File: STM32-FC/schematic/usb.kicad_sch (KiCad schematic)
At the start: 26 parts, among them J2 USB_C_USB2.0_16P, J3 BM06B-GHS-TBT, U1 USBLC6-2SC6, U2 TPS62840YBG, U3 TPS62840YBG, U4 TPS62840YBG

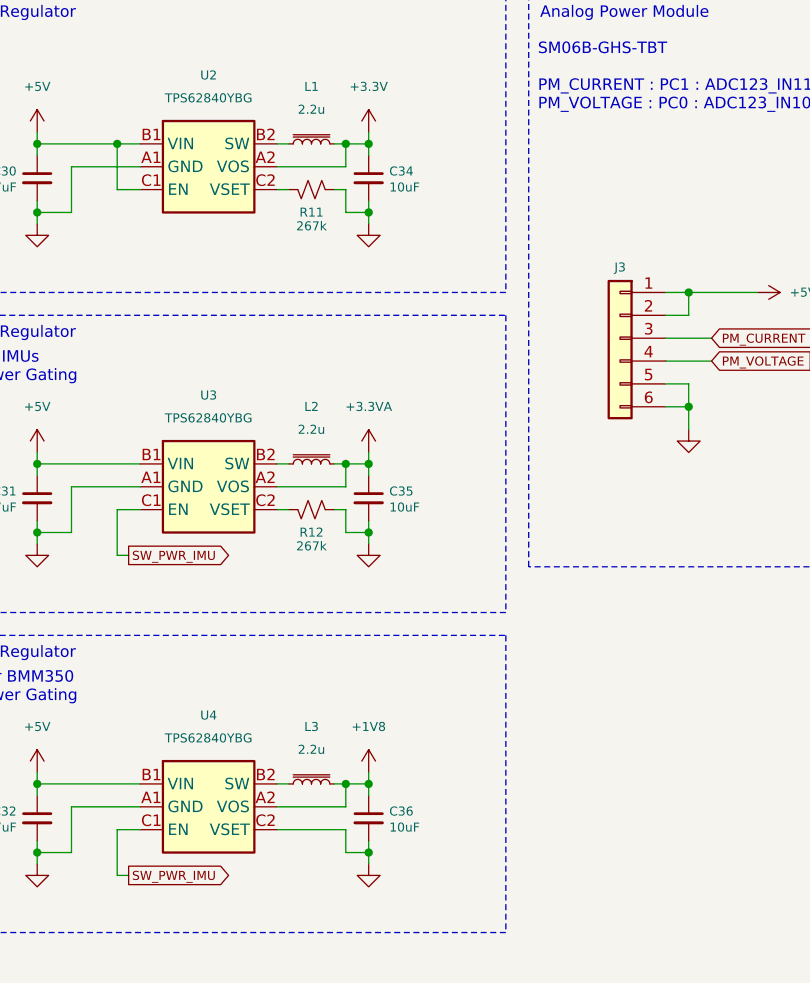
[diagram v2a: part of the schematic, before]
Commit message: change : RC size 0402 to 0201
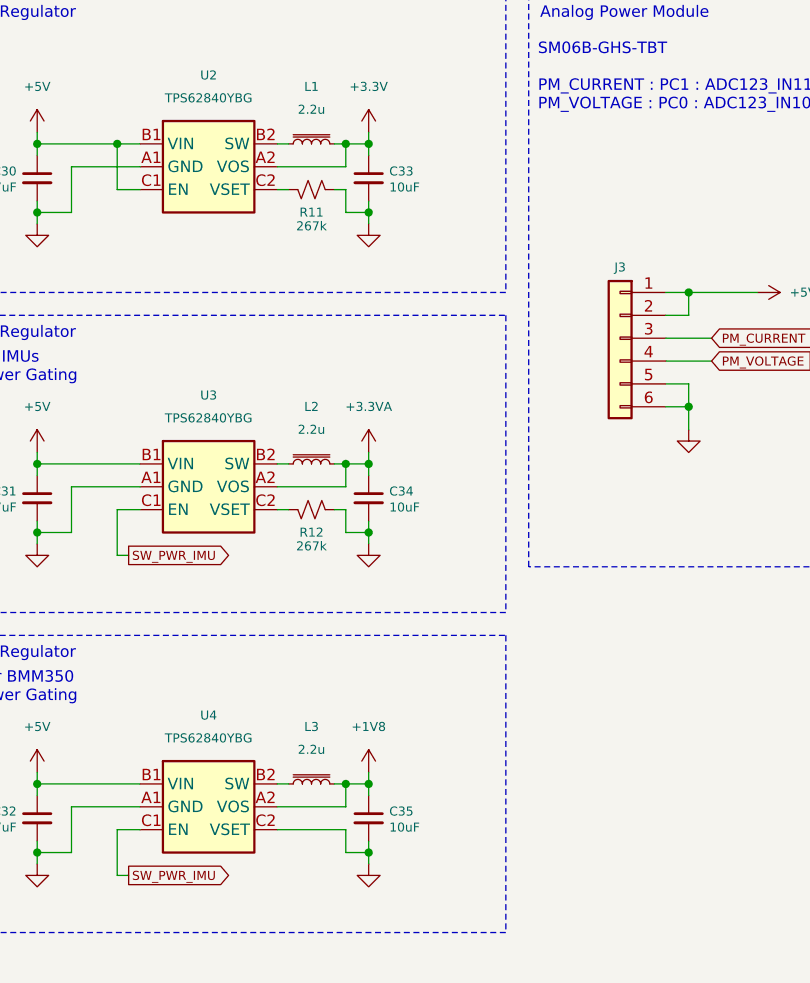
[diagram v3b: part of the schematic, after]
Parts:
- renumbered C34 to C33, C35 to C34, C36 to C35
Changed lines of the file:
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@@
 		(dnp no)
 		(fields_autoplaced yes)
-		(property "Reference" "#PWR049"
+		(property "Reference" "#PWR048"
 			(at 187.96 31.75 0)
 			(effects
@@
 			(project ""
 				(path "/8d4cc317-3933-4aa6-844b-8c5c635e89c7/a4ea5d55-2314-4804-8750-f8f12484bbce"
-					(reference "#PWR049")
+					(reference "#PWR048")
 					(unit 1)
 				)
@@
 		(on_board yes)
 		(dnp no)
-		(property "Reference" "#PWR058"
+		(property "Reference" "#PWR055"
 			(at 227.33 45.72 0)
 			(effects
@@
 			(project ""
 				(path "/8d4cc317-3933-4aa6-844b-8c5c635e89c7/a4ea5d55-2314-4804-8750-f8f12484bbce"
-					(reference "#PWR058")
+					(reference "#PWR055")
 					(unit 1)
 				)
@@
 		(dnp no)
 		(fields_autoplaced yes)
-		(property "Reference" "#PWR045"
+		(property "Reference" "#PWR046"
 			(at 151.13 102.87 0)
 			(effects
@@
 			(project "STM32-FC"
 				(path "/8d4cc317-3933-4aa6-844b-8c5c635e89c7/a4ea5d55-2314-4804-8750-f8f12484bbce"
-					(reference "#PWR045")
+					(reference "#PWR046")
 					(unit 1)
 				)
@@
 		(dnp no)
 		(fields_autoplaced yes)
-		(property "Reference" "#PWR042"
+		(property "Reference" "#PWR043"
 			(at 151.13 44.45 0)
 			(effects
@@
 			(project ""
 				(path "/8d4cc317-3933-4aa6-844b-8c5c635e89c7/a4ea5d55-2314-4804-8750-f8f12484bbce"
-					(reference "#PWR042")
+					(reference "#PWR043")
 					(unit 1)
 				)
@@
 		(on_board yes)
 		(dnp no)
-		(property "Reference" "#FLG05"
+		(property "Reference" "#FLG06"
 			(at 113.665 31.75 0)
 			(effects
@@
 			(project "STM32-FC"
 				(path "/8d4cc317-3933-4aa6-844b-8c5c635e89c7/a4ea5d55-2314-4804-8750-f8f12484bbce"
-					(reference "#FLG05")
+					(reference "#FLG06")
 					(unit 1)
 				)
@@
 		(dnp no)
 		(fields_autoplaced yes)
-		(property "Reference" "#PWR041"
+		(property "Reference" "#PWR042"
 			(at 151.13 31.75 0)
 			(effects
@@
 			(project ""
 				(path "/8d4cc317-3933-4aa6-844b-8c5c635e89c7/a4ea5d55-2314-4804-8750-f8f12484bbce"
-					(reference "#PWR041")
+					(reference "#PWR042")
 					(unit 1)
 				)
@@
 		(dnp no)
 		(fields_autoplaced yes)
-		(property "Reference" "#PWR040"
+		(property "Reference" "#PWR041"
 			(at 104.14 31.75 0)
 			(effects
@@
 			(project "STM32-FC"
 				(path "/8d4cc317-3933-4aa6-844b-8c5c635e89c7/a4ea5d55-2314-4804-8750-f8f12484bbce"
-					(reference "#PWR040")
+					(reference "#PWR041")
 					(unit 1)
 				)
@@
 		(dnp no)
 		(fields_autoplaced yes)
-		(property "Reference" "#PWR046"
+		(property "Reference" "#PWR047"
 			(at 151.13 115.57 0)
 			(effects
@@
 			(project "STM32-FC"
 				(path "/8d4cc317-3933-4aa6-844b-8c5c635e89c7/a4ea5d55-2314-4804-8750-f8f12484bbce"
-					(reference "#PWR046")
+					(reference "#PWR047")
 					(unit 1)
 				)
@@
 		(on_board yes)
 		(dnp no)
-		(property "Reference" "#FLG03"
+		(property "Reference" "#FLG04"
 			(at 113.665 26.67 0)
 			(effects
@@
 			(project "STM32-FC"
 				(path "/8d4cc317-3933-4aa6-844b-8c5c635e89c7/a4ea5d55-2314-4804-8750-f8f12484bbce"
-					(reference "#FLG03")
+					(reference "#FLG04")
 					(unit 1)
 				)
@@
 		(on_board yes)
 		(dnp no)
-		(property "Reference" "#PWR038"
+		(property "Reference" "#PWR039"
 			(at 114.3 26.67 0)
 			(effects
@@
 			(project "STM32-FC"
 				(path "/8d4cc317-3933-4aa6-844b-8c5c635e89c7/a4ea5d55-2314-4804-8750-f8f12484bbce"
-					(reference "#PWR038")
+					(reference "#PWR039")
 					(unit 1)
 				)
@@
 		(on_board yes)
 		(dnp no)
-		(property "Reference" "#PWR048"
+		(property "Reference" "#PWR038"
 			(at 114.3 24.13 0)
 			(effects
@@
 			(project "STM32-FC"
 				(path "/8d4cc317-3933-4aa6-844b-8c5c635e89c7/a4ea5d55-2314-4804-8750-f8f12484bbce"
-					(reference "#PWR048")
+					(reference "#PWR038")
 					(unit 1)
 				)
@@
 		(dnp no)
 		(fields_autoplaced yes)
-		(property "Reference" "#PWR043"
+		(property "Reference" "#PWR044"
 			(at 151.13 67.31 0)
 			(effects
@@
 			(project ""
 				(path "/8d4cc317-3933-4aa6-844b-8c5c635e89c7/a4ea5d55-2314-4804-8750-f8f12484bbce"
-					(reference "#PWR043")
+					(reference "#PWR044")
 					(unit 1)
 				)
@@
 		(dnp no)
 		(fields_autoplaced yes)
-		(property "Reference" "#PWR047"
+		(property "Reference" "#PWR050"
 			(at 187.96 67.31 0)
 			(effects
@@
 			(project ""
 				(path "/8d4cc317-3933-4aa6-844b-8c5c635e89c7/a4ea5d55-2314-4804-8750-f8f12484bbce"
-					(reference "#PWR047")
+					(reference "#PWR050")
 					(unit 1)
 				)
@@
 		(on_board yes)
 		(dnp no)
-		(property "Reference" "C36"
+		(property "Reference" "C35"
 			(at 190.246 103.378 0)
 			(effects
@@
 			(project "STM32-FC"
 				(path "/8d4cc317-3933-4aa6-844b-8c5c635e89c7/a4ea5d55-2314-4804-8750-f8f12484bbce"
-					(reference "C36")
+					(reference "C35")
 					(unit 1)
 				)
@@
 		(on_board yes)
 		(dnp no)
-		(property "Reference" "#PWR039"
+		(property "Reference" "#PWR040"
 			(at 114.3 29.21 0)
 			(effects
@@
 			(project "STM32-FC"
 				(path "/8d4cc317-3933-4aa6-844b-8c5c635e89c7/a4ea5d55-2314-4804-8750-f8f12484bbce"
-					(reference "#PWR039")
+					(reference "#PWR040")
 					(unit 1)
 				)
@@
 		(dnp no)
 		(fields_autoplaced yes)
-		(property "Reference" "#PWR057"
+		(property "Reference" "#PWR054"
 			(at 223.52 67.31 0)
 			(effects
@@
 			(project ""
 				(path "/8d4cc317-3933-4aa6-844b-8c5c635e89c7/a4ea5d55-2314-4804-8750-f8f12484bbce"
-					(reference "#PWR057")
+					(reference "#PWR054")
 					(unit 1)
 				)
@@
 		(on_board yes)
 		(dnp no)
-		(property "Reference" "#FLG07"
+		(property "Reference" "#FLG03"
 			(at 113.665 24.13 0)
 			(effects
@@
 			(project "STM32-FC"
 				(path "/8d4cc317-3933-4aa6-844b-8c5c635e89c7/a4ea5d55-2314-4804-8750-f8f12484bbce"
-					(reference "#FLG07")
+					(reference "#FLG03")
 					(unit 1)
 				)
@@
 		(on_board yes)
 		(dnp no)
-		(property "Reference" "#FLG04"
+		(property "Reference" "#FLG05"
 			(at 113.665 29.21 0)
 			(effects
@@
 			(project "STM32-FC"
 				(path "/8d4cc317-3933-4aa6-844b-8c5c635e89c7/a4ea5d55-2314-4804-8750-f8f12484bbce"
-					(reference "#FLG04")
+					(reference "#FLG05")
 					(unit 1)
 				)
@@
 		(dnp no)
 		(fields_autoplaced yes)
-		(property "Reference" "#PWR054"
+		(property "Reference" "#PWR053"
 			(at 187.96 115.57 0)
 			(effects
@@
 			(project "STM32-FC"
 				(path "/8d4cc317-3933-4aa6-844b-8c5c635e89c7/a4ea5d55-2314-4804-8750-f8f12484bbce"
-					(reference "#PWR054")
+					(reference "#PWR053")
 					(unit 1)
 				)
@@
 		(on_board yes)
 		(dnp no)
-		(property "Reference" "C35"
+		(property "Reference" "C34"
 			(at 190.246 67.818 0)
 			(effects
@@
 			(project "STM32-FC"
 				(path "/8d4cc317-3933-4aa6-844b-8c5c635e89c7/a4ea5d55-2314-4804-8750-f8f12484bbce"
-					(reference "C35")
+					(reference "C34")
 					(unit 1)
 				)
@@
 		(dnp no)
 		(fields_autoplaced yes)
-		(property "Reference" "#PWR044"
+		(property "Reference" "#PWR045"
 			(at 151.13 80.01 0)
 			(effects
@@
 			(project ""
 				(path "/8d4cc317-3933-4aa6-844b-8c5c635e89c7/a4ea5d55-2314-4804-8750-f8f12484bbce"
-					(reference "#PWR044")
+					(reference "#PWR045")
 					(unit 1)
 				)
@@
 		(on_board yes)
 		(dnp no)
-		(property "Reference" "#PWR053"
+		(property "Reference" "#PWR052"
 			(at 187.96 102.87 0)
 			(effects
@@
 			(project "STM32-FC"
 				(path "/8d4cc317-3933-4aa6-844b-8c5c635e89c7/a4ea5d55-2314-4804-8750-f8f12484bbce"
-					(reference "#PWR053")
+					(reference "#PWR052")
 					(unit 1)
 				)
@@
 		(on_board yes)
 		(dnp no)
-		(property "Reference" "C34"
+		(property "Reference" "C33"
 			(at 190.246 32.258 0)
 			(effects
@@
 			(project "STM32-FC"
 				(path "/8d4cc317-3933-4aa6-844b-8c5c635e89c7/a4ea5d55-2314-4804-8750-f8f12484bbce"
-					(reference "C34")
+					(reference "C33")
 					(unit 1)
 				)
@@
 		(dnp no)
 		(fields_autoplaced yes)
-		(property "Reference" "#PWR052"
+		(property "Reference" "#PWR051"
 			(at 187.96 80.01 0)
 			(effects
@@
 			(project "STM32-FC_v2"
 				(path "/8d4cc317-3933-4aa6-844b-8c5c635e89c7/a4ea5d55-2314-4804-8750-f8f12484bbce"
-					(reference "#PWR052")
+					(reference "#PWR051")
 					(unit 1)
 				)
@@
 		(dnp no)
 		(fields_autoplaced yes)
-		(property "Reference" "#PWR050"
+		(property "Reference" "#PWR049"
 			(at 187.96 44.45 0)
 			(effects
@@
 			(project "STM32-FC_v2"
 				(path "/8d4cc317-3933-4aa6-844b-8c5c635e89c7/a4ea5d55-2314-4804-8750-f8f12484bbce"
-					(reference "#PWR050")
+					(reference "#PWR049")
 					(unit 1)
 				)
